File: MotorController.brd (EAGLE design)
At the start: 100.4 x 41.1 mm, 13 parts

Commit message: pcb design waiting for inspection
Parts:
- moved J4 9.46 mm to (41.0, 31.0)
- moved J3 9.35 mm to (41.0, 37.6)
- moved U$2 8.90 mm to (64.1, 28.7)
- moved J5 6.95 mm to (4.57, 4.95), flipped to the bottom, turned to 180 degrees
- moved J2 5.39 mm to (4.45, 37.6)
- moved U$1 5.34 mm to (27.2, 28.7)
- moved J1 5.34 mm to (4.45, 31.0)
- moved CON1 4.73 mm to (86.7, 30.0)
- moved C2 3.49 mm to (50.2, 22.9)
- moved U$4 3.30 mm to (31.9, 8.89)
- moved U$6 2.37 mm to (93.7, 19.7), flipped to the bottom
- moved C3 2.32 mm to (13.2, 22.9)
- moved U$5 2.29 mm to (69.6, 8.89)
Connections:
- removed net 5V: CON1.8, U$6.P$4
- removed net N$14: U$2.EN_N
- removed net N$9: U$1.EN_N
- net GND: now also U$1.EN_N, U$2.EN_N, U$6.P$3
- net VBAT: now also U$6.P$1; no longer U$6.P$3
- net VCC: now also CON1.8, U$6.P$4
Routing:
- net VCC: track 0.00 -> 110.5 mm, vias 0 -> 4
- net M_DIR2: track 16.6 -> 73.4 mm, vias 0 -> 2
- net M_STEP2: track 14.8 -> 67.6 mm, vias 0 -> 2
- net GND: track 0.00 -> 28.9 mm, vias 0 -> 6
- net M_DIR1: track 4.34 -> 30.5 mm, vias 0 -> 2
- net M_STEP1: track 2.54 -> 25.4 mm, vias 0 -> 2
- net M_M0: track 56.3 -> 78.6 mm, vias 0 -> 2
- net M_M1: track 52.5 -> 74.1 mm, vias 0 -> 2
- net M_M2: track 57.2 -> 78.4 mm, vias 0 -> 2
- net 5V: track 17.3 -> 0.00 mm
- net VMOT2: track 38.2 -> 44.2 mm, vias 2 -> 0
- net VMOT1: track 37.1 -> 42.2 mm
- net SIDEA_B2: track 25.7 -> 27.0 mm
- net SIDEA_B1: track 20.3 -> 21.4 mm
- net SIDEB_B2: track 26.6 -> 27.3 mm
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- added copper zone on layer 1, net GND
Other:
- board size 100.4 x 41.1 mm -> 100.4 x 40.9 mm
- board text added: "2020"
- board text added: "Nirgu"
- board text added: "legokor"

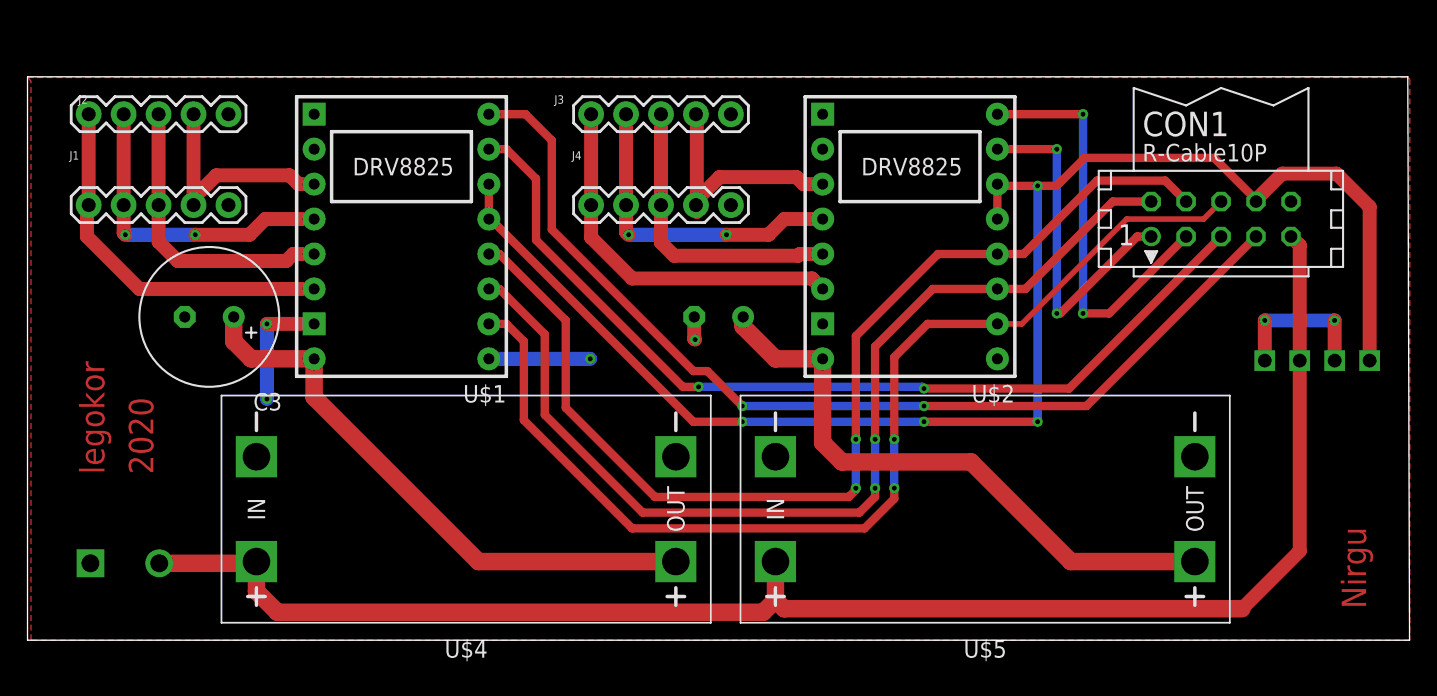
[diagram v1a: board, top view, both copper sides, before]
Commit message: fixing points added, overall pcb width modified, cable connections changed
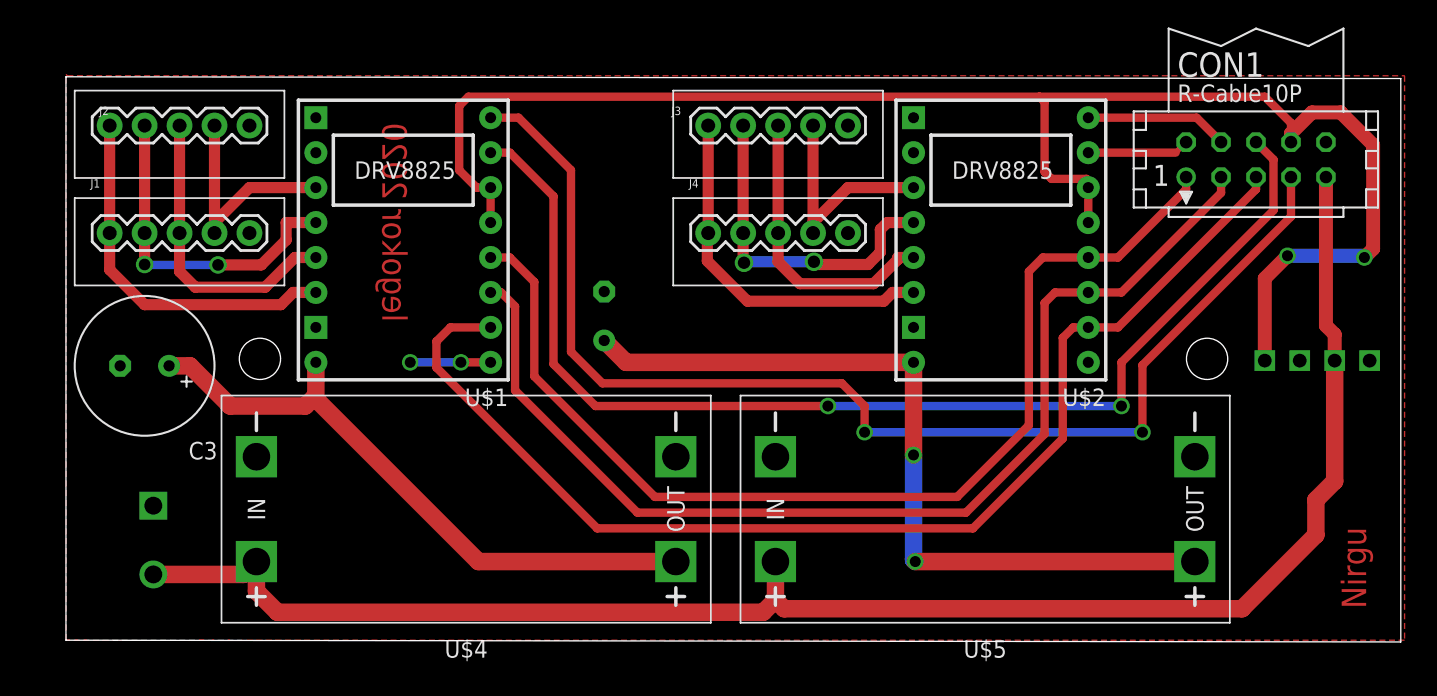
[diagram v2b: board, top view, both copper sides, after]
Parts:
- J1, J2, J3, J4: device SparkFun-Connectors:1X05 -> custom:1X05
- moved J4 8.75 mm to (49.5, 29.0)
- moved J3 8.55 mm to (49.5, 36.8)
- moved C2 8.32 mm to (41.9, 22.9), turned to 90 degrees
- moved U$2 6.61 mm to (70.7, 28.4)
- moved J5 6.20 mm to (9.14, 9.14), turned to 270 degrees
- moved C3 5.89 mm to (8.51, 19.3)
- moved CON1 5.01 mm to (89.3, 34.3)
- moved J1 2.54 mm to (5.97, 29.0)
- moved J2 1.73 mm to (5.97, 36.8)
- moved U$1 0.28 mm to (27.3, 28.4)
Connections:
- net GND: now also U$6.P$1, U$6.P$4; no longer U$6.P$2, U$6.P$3
- net M_DIR1: now also CON1.4; no longer CON1.3
- net M_M0: now also CON1.5; no longer CON1.6
- net M_M1: now also CON1.3; no longer CON1.2
- net M_M2: now also CON1.1; no longer CON1.4
- net M_STEP1: now also CON1.2; no longer CON1.1
- net M_STEP2: now also CON1.6; no longer CON1.5
- net VBAT: now also U$6.P$2; no longer U$6.P$1
- net VCC: now also U$6.P$3; no longer U$6.P$4
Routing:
- net GND: track 28.9 -> 67.8 mm, vias 6 -> 2
- net M_DIR1: track 30.5 -> 10.4 mm, vias 2 -> 0
- net M_STEP1: track 25.4 -> 7.43 mm, vias 2 -> 0
- net M_STEP2: track 67.6 -> 84.9 mm
- net M_DIR2: track 73.4 -> 88.7 mm
- net VMOT2: track 44.2 -> 58.0 mm, vias 0 -> 2
- net M_M0: track 78.6 -> 86.0 mm, vias 2 -> 0
- net VBAT: track 114.0 -> 120.3 mm
- net M_M1: track 74.1 -> 79.6 mm, vias 2 -> 0
- net VCC: track 110.5 -> 115.8 mm, vias 4 -> 2
- net VMOT1: track 42.2 -> 45.9 mm
- net SIDEA_A1: track 23.0 -> 24.6 mm
- net SIDEB_A2: track 17.6 -> 16.2 mm
- net SIDEB_A1: track 23.4 -> 24.7 mm
- net SIDEB_B2: track 27.3 -> 26.3 mm
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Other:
- board size 100.4 x 40.9 mm -> 97 x 41.1 mm
- board text added: "legokor 2020"
- board text removed: "2020"
- board text removed: "legokor"

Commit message: via drill size enlarged
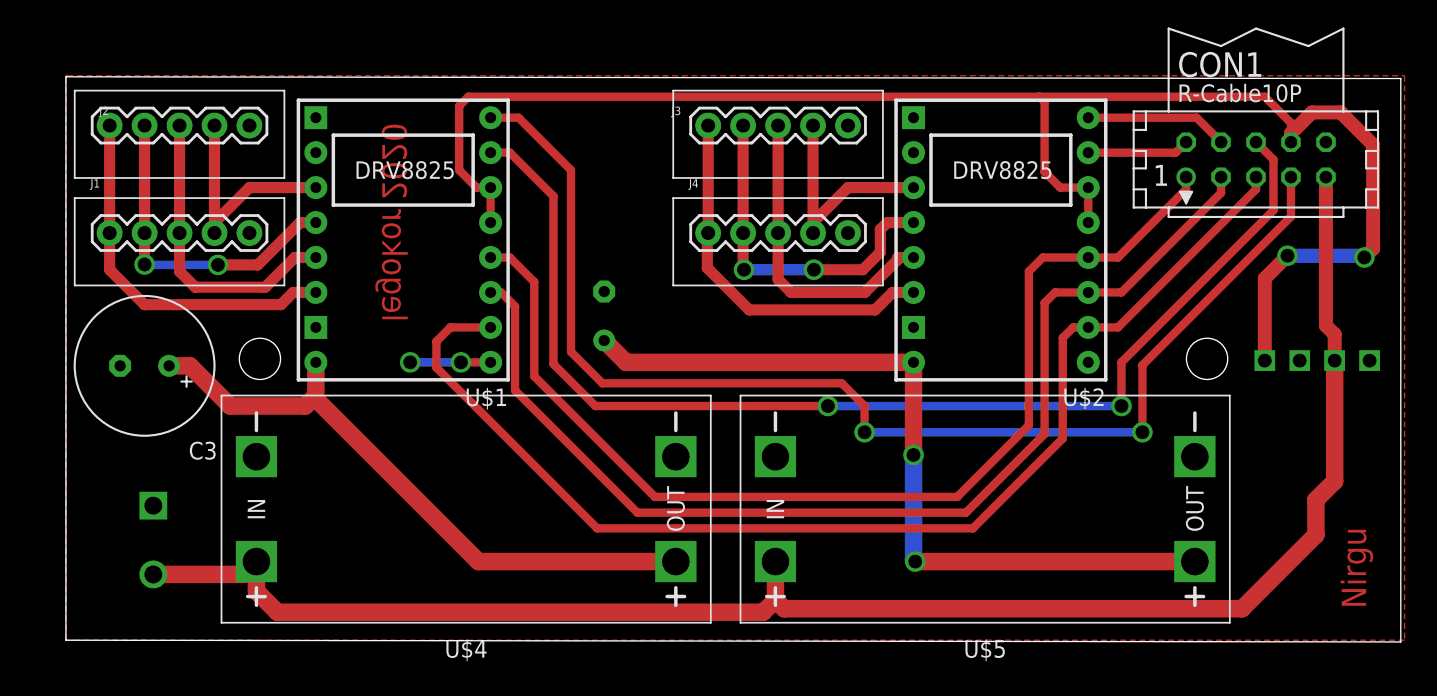
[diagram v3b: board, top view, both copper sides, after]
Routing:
- net SIDEB_B1: track 21.3 -> 22.6 mm
- net SIDEB_B2: track 26.3 -> 27.2 mm
- net SIDEA_A1: track 24.6 -> 23.8 mm
- net GND: track 67.8 -> 68.6 mm
- net SIDEB_A1: track 24.7 -> 25.2 mm
